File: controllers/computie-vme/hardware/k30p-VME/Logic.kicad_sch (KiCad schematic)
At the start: 7 parts, among them J5 JTAG, U4 ATF1504AS-10JU84

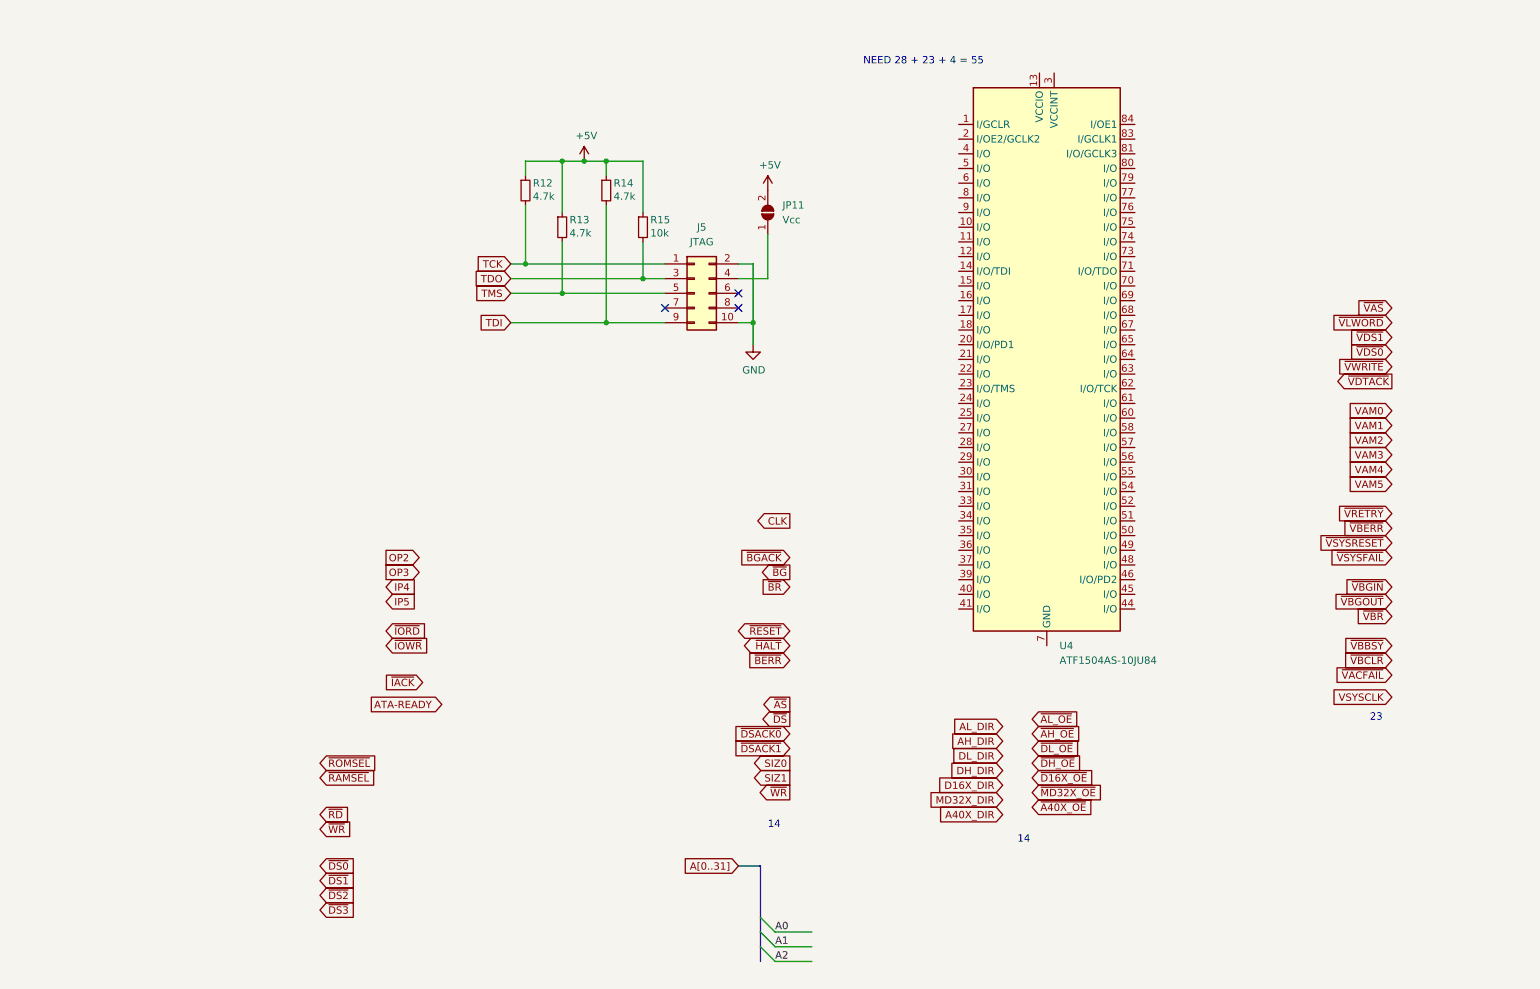
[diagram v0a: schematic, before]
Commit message: Added SystemBoardSMT, renamed k30 boards, and added progress
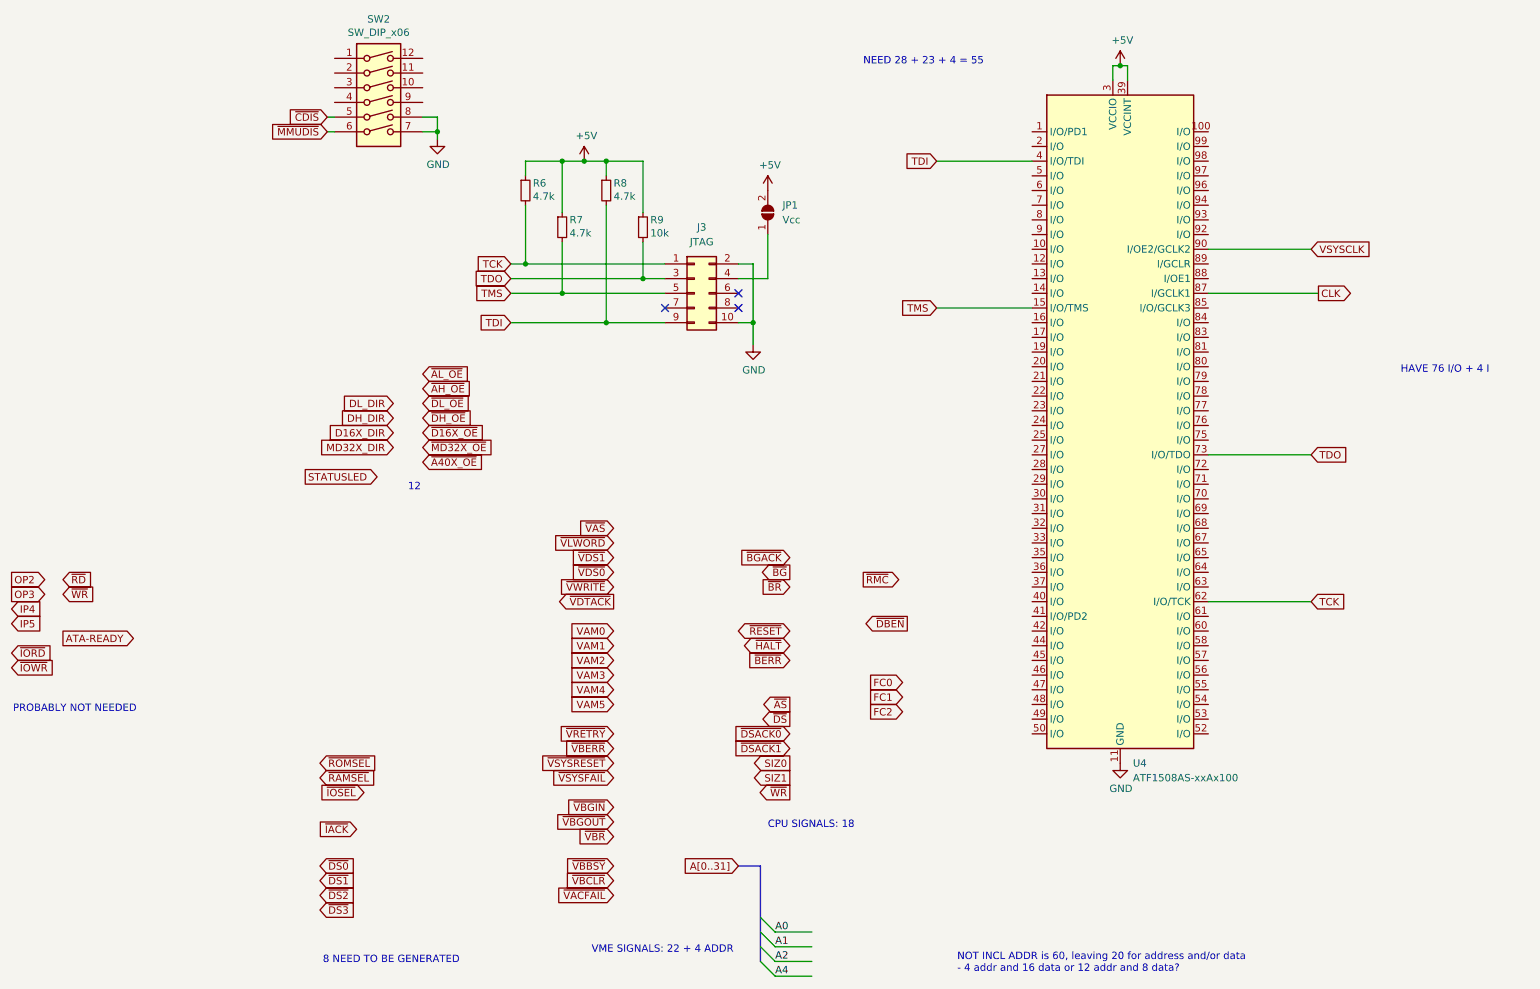
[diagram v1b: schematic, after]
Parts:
- removed U4: ATF1504AS-10JU84, Package_LCC:PLCC-84_THT-Socket, symbol Computie_CPLDs:ATF1504AS-10JU84
- added SW2: SW_DIP_x06, Package_DIP:DIP-12_W7.62mm_LongPads, symbol Switch:SW_DIP_x06
- added U4: ATF1508AS-xxAx100, Package_QFP:TQFP-100_14x14mm_P0.5mm, symbol Computie_CPLDs:ATF1508AS-xxAx100
- R6: renamed from R12; footprint Resistor_THT:R_Axial_DIN0204_L3.6mm_D1.6mm_P5.08mm_Horizontal -> Resistor_SMD:R_0805_2012Metric_Pad1.20x1.40mm_HandSolder
- R7: renamed from R13; footprint Resistor_THT:R_Axial_DIN0204_L3.6mm_D1.6mm_P5.08mm_Horizontal -> Resistor_SMD:R_0805_2012Metric_Pad1.20x1.40mm_HandSolder
- R8: renamed from R14; footprint Resistor_THT:R_Axial_DIN0204_L3.6mm_D1.6mm_P5.08mm_Horizontal -> Resistor_SMD:R_0805_2012Metric_Pad1.20x1.40mm_HandSolder
- R9: renamed from R15; footprint Resistor_THT:R_Axial_DIN0204_L3.6mm_D1.6mm_P5.08mm_Horizontal -> Resistor_SMD:R_0805_2012Metric_Pad1.20x1.40mm_HandSolder
- renumbered J5 to J3, JP11 to JP1
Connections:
- net +5V: now also U4.18 (VCCIO), U4.3 (VCCIO), U4.34 (VCCIO), U4.39 (VCCINT), U4.51 (VCCIO), U4.66 (VCCIO), U4.82 (VCCIO), U4.91 (VCCINT)
- net CLK: now also U4.87 (I/GCLK1)
- net GND: now also SW2.7, SW2.8, U4.11 (GND), U4.26 (GND), U4.38 (GND), U4.43 (GND), U4.59 (GND), U4.74 (GND), U4.86 (GND), U4.95 (GND)
- net TCK: now also U4.62 (I/O/TCK)
- net TDI: now also U4.4 (I/O/TDI)
- net TDO: now also U4.73 (I/O/TDO)
- net TMS: now also U4.15 (I/O/TMS)
- net VSYSCLK: now also U4.90 (I/OE2/GCLK2)
- new net ~{CDIS}: SW2.5
- new net ~{MMUDIS}: SW2.6
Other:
- note added: "12"
- note added: "8 NEED TO BE GENERATED"
- note added: "CPU SIGNALS: 18"
- note added: "HAVE 76 I/O + 4 I"
- note added: "NOT INCL ADDR is 60, leaving 20 for address and/or data - 4 addr and 16 data or 12 addr and 8 data?"
- note added: "PROBABLY NOT NEEDED"
- note added: "VME SIGNALS: 22 + 4 ADDR"
- note removed: "14"
- note removed: "23"

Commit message: Updating with more work in progress
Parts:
- removed SW2: SW_DIP_x06, Package_DIP:DIP-12_W7.62mm_LongPads, symbol Switch:SW_DIP_x06
- renumbered JP1 to JP3
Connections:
- net D16X_DIR: now also U4.94 (I/O)
- net DL_DIR: now also U4.97 (I/O)
- net MD32X_DIR: now also U4.92 (I/O)
- net STATUSLED: now also U4.52 (I/O)
- net ~{A40X_OE}: now also U4.99 (I/O)
- net ~{AL_OE}: now also U4.100 (I/O)
- net ~{D16X_OE}: now also U4.96 (I/O)
- net ~{DL_OE}: now also U4.98 (I/O)
- net ~{MD32X_OE}: now also U4.93 (I/O)
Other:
- note added: "NOT INCL ADDR is 57, leaving 23 for address and/or data - 4 addr and 16 data or 12 addr and 8 data?"
- note removed: "12"
- note removed: "8 NEED TO BE GENERATED"
- note removed: "NOT INCL ADDR is 60, leaving 20 for address and/or data - 4 addr and 16 data or 12 addr and 8 data?"
- note removed: "PROBABLY NOT NEEDED"
- title: k30-VME32 -> k30p-VME

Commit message: Reorganized a bit
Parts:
- added U17: 74LS30, symbol 74xx:74LS30
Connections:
- net CPU_CLK: now reaches U4.84 (I/O)
- net CLK renamed MAIN_CLK
- new net LA24: U17.1
- new net LA25: U17.2
- new net LA26: U17.3
- new net LA27: U17.4
- new net LA28: U17.5
- new net LA29: U17.6
- new net LA30: U17.11
- new net LA31: U17.12
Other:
- note added: "15 in the reduced configuration"
- note added: "54 REQUIRED (+1 if you add RAMSEL)"
- note added: "68 I/Os REMAINING"
- note added: "If you add these from the serial port controller, it would give you some flags that could be set by the program, to change the selected bus access type"
- note added: "LOW PRIORITY SIGNALS: CPU VME LOCAL"
- note added: "MED PRIORITY SIGNALS: CPU VME LOCAL"
- note added: "OR"
- note added: "REQUIRED SIGNALS: CPU VME LOCAL"
- note added: "You need the data lines if you want to set an interrupt vector when the VME bus is making one or else I *think* you can use AVEC to make it use specific hardware vectors numbers"
- note added: "these 4 signals differentiate between breakpoint ack, interrupt ack, and coproc"
- note removed: "CPU SIGNALS: 18"
- note removed: "HAVE 76 I/O + 4 I"
- note removed: "VME SIGNALS: 22 + 4 ADDR"
- moved on the sheet: J3, JP3, R6, R7, R8, R9, U4

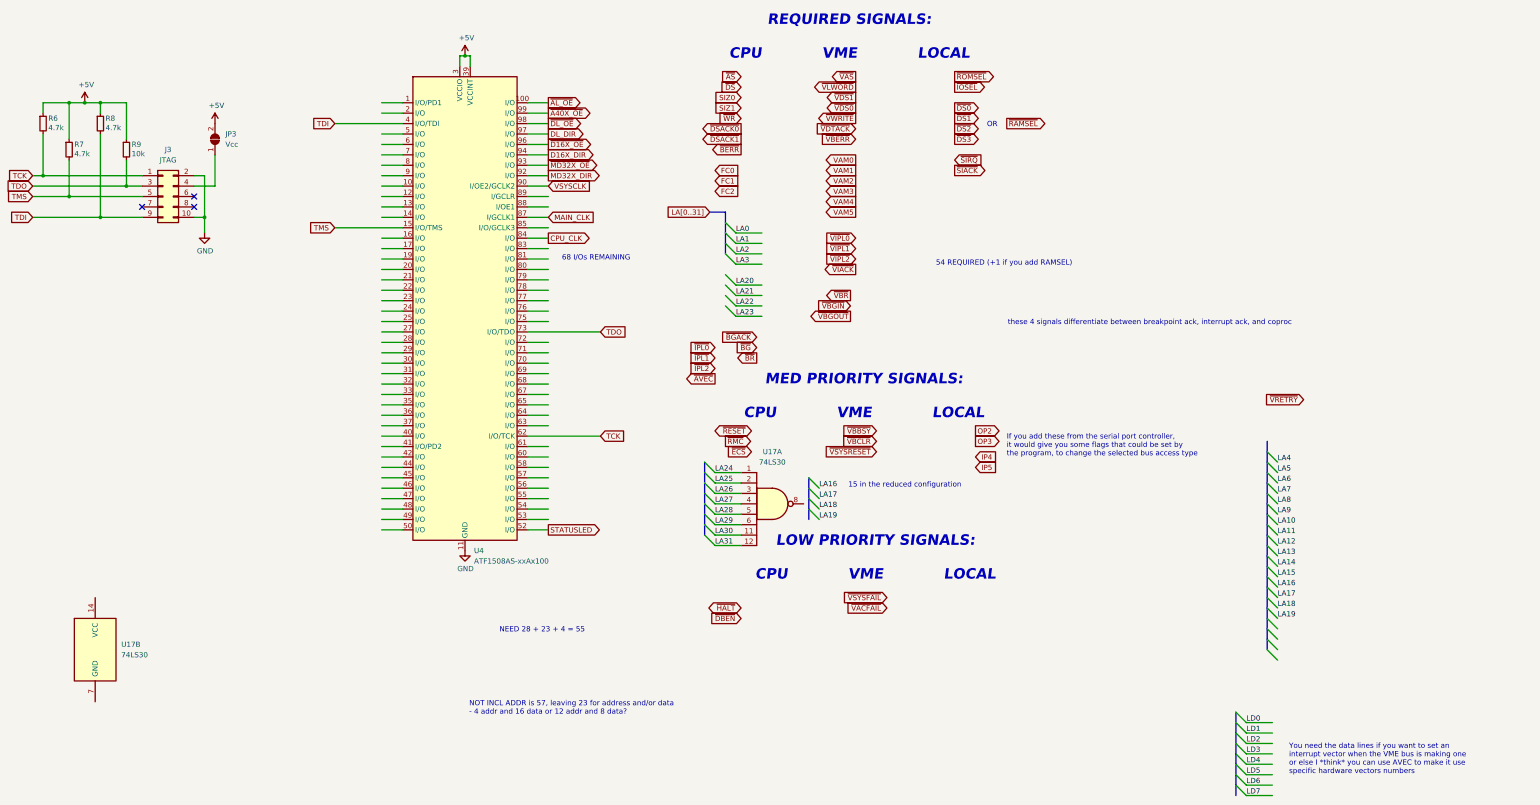
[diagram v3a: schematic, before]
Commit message: Basic systemboard logic for bus arbitration is working and tested
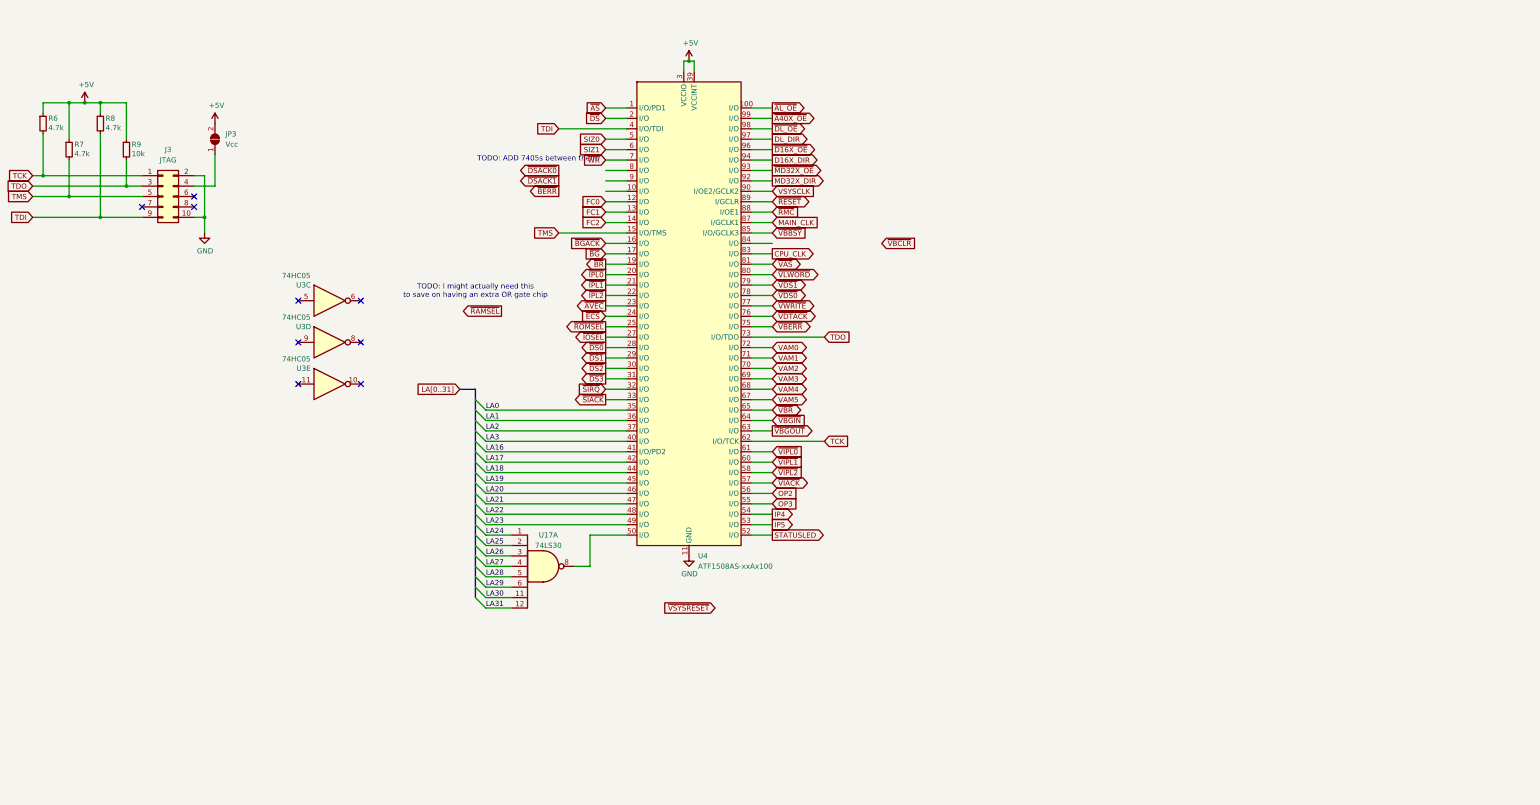
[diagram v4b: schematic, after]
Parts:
- removed unit 2 of U17
- added U3: 74HC05, Package_SO:TSSOP-14_4.4x5mm_P0.65mm, symbol 74xx:74LS05
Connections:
- net CPU_CLK: now also U4.83 (I/O); no longer U4.84 (I/O)
- net FC0: now also U4.12 (I/O)
- net FC1: now also U4.13 (I/O)
- net FC2: now also U4.14 (I/O)
- net IP4: now also U4.54 (I/O)
- net IP5: now also U4.53 (I/O)
- net LA0: now also U4.35 (I/O)
- net LA1: now also U4.36 (I/O)
- net LA16: now also U4.41 (I/O/PD2)
- net LA17: now also U4.42 (I/O)
- net LA18: now also U4.44 (I/O)
- net LA19: now also U4.45 (I/O)
- net LA2: now also U4.37 (I/O)
- net LA20: now also U4.46 (I/O)
- net LA21: now also U4.47 (I/O)
- net LA22: now also U4.48 (I/O)
- net LA23: now also U4.49 (I/O)
- net LA3: now also U4.40 (I/O)
- net OP2: now also U4.56 (I/O)
- net OP3: now also U4.55 (I/O)
- net SIZ0: now also U4.5 (I/O)
- net SIZ1: now also U4.6 (I/O)
- net VAM0: now also U4.72 (I/O)
- net VAM1: now also U4.71 (I/O)
- net VAM2: now also U4.70 (I/O)
- net VAM3: now also U4.69 (I/O)
- net VAM4: now also U4.68 (I/O)
- net VAM5: now also U4.67 (I/O)
- net ~{AS}: now also U4.1 (I/O/PD1)
- net ~{AVEC}: now also U4.23 (I/O)
- net ~{BGACK}: now also U4.16 (I/O)
- net ~{BG}: now also U4.17 (I/O)
- net ~{BR}: now also U4.19 (I/O)
- net ~{DS0}: now also U4.28 (I/O)
- net ~{DS1}: now also U4.29 (I/O)
- net ~{DS2}: now also U4.30 (I/O)
- net ~{DS3}: now also U4.31 (I/O)
- net ~{DS}: now also U4.2 (I/O)
- net ~{ECS}: now also U4.24 (I/O)
- net ~{IOSEL}: now also U4.27 (I/O)
- net ~{IPL0}: now also U4.20 (I/O)
- net ~{IPL1}: now also U4.21 (I/O)
- net ~{IPL2}: now also U4.22 (I/O)
- net ~{RESET}: now also U4.89 (I/GCLR)
- net ~{RMC}: now also U4.88 (I/OE1)
- net ~{ROMSEL}: now also U4.25 (I/O)
- net ~{SIACK}: now also U4.33 (I/O)
- net ~{SIRQ}: now also U4.32 (I/O)
- net ~{VAS}: now also U4.81 (I/O)
- net ~{VBBSY}: now also U4.85 (I/O/GCLK3)
- net ~{VBERR}: now also U4.75 (I/O)
- net ~{VBGIN}: now also U4.64 (I/O)
- net ~{VBGOUT}: now also U4.63 (I/O)
- net ~{VBR}: now also U4.65 (I/O)
- net ~{VDS0}: now also U4.78 (I/O)
- net ~{VDS1}: now also U4.79 (I/O)
- net ~{VDTACK}: now also U4.76 (I/O)
- net ~{VIACK}: now also U4.57 (I/O)
- net ~{VIPL0}: now also U4.61 (I/O)
- net ~{VIPL1}: now also U4.60 (I/O)
- net ~{VIPL2}: now also U4.58 (I/O)
- net ~{VLWORD}: now also U4.80 (I/O)
- net ~{VWRITE}: now also U4.77 (I/O)
- net ~{WR}: now also U4.7 (I/O)
- net at U17.8: now also U4.50 (I/O)
- no-connect marks 3 -> 9
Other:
- note added: "TODO: ADD 7405s between them?"
- note added: "TODO: I might actually need this to save on having an extra OR gate chip"
- note removed: "15 in the reduced configuration"
- note removed: "54 REQUIRED (+1 if you add RAMSEL)"
- note removed: "68 I/Os REMAINING"
- note removed: "If you add these from the serial port controller, it would give you some flags that could be set by the program, to change the selected bus access type"
- note removed: "LOW PRIORITY SIGNALS: CPU VME LOCAL"
- note removed: "MED PRIORITY SIGNALS: CPU VME LOCAL"
- note removed: "NEED 28 + 23 + 4 = 55"
- note removed: "NOT INCL ADDR is 57, leaving 23 for address and/or data - 4 addr and 16 data or 12 addr and 8 data?"
- note removed: "OR"
- note removed: "REQUIRED SIGNALS: CPU VME LOCAL"
- note removed: "You need the data lines if you want to set an interrupt vector when the VME bus is making one or else I *think* you can use AVEC to make it use specific hardware vectors numbers"
- note removed: "these 4 signals differentiate between breakpoint ack, interrupt ack, and coproc"
- moved on the sheet: U17A, U4
